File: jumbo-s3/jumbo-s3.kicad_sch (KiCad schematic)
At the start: 21 parts, among them U1 ESP32-S3, U2 APS12808L-3OBM-BA, U3 W25Q128JVS

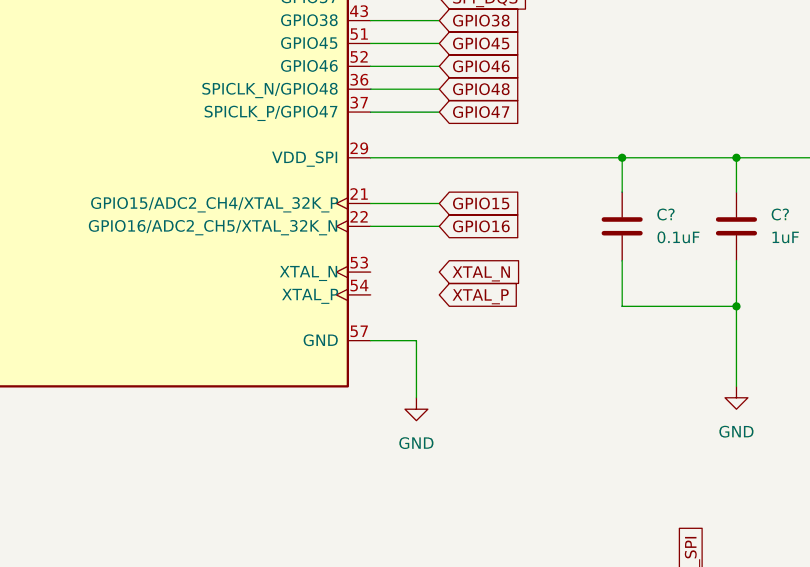
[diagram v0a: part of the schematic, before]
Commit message: schematic: add uC, flash and PSRAM
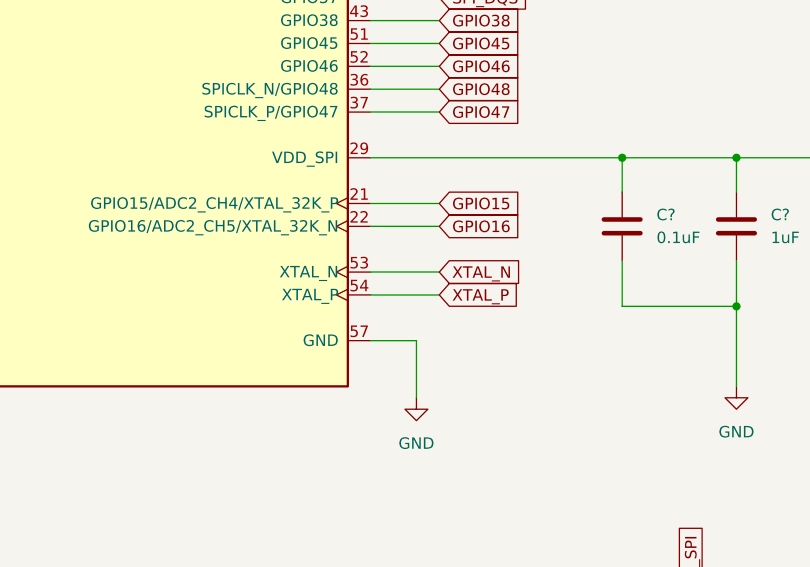
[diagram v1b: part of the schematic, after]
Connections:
- net XTAL_N: now also U1.53 (XTAL_N)
- net XTAL_P: now also U1.54 (XTAL_P)
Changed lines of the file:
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@@
+    (stroke (width 0) (type default) (color 0 0 0 0))
+  )
+  (wire (pts (xy 134.62 100.33) (xy 142.24 100.33))
     (stroke (width 0) (type default) (color 0 0 0 0))
   )
@@
     (stroke (width 0) (type default) (color 0 0 0 0))
   )
+  (wire (pts (xy 134.62 102.87) (xy 142.24 102.87))
+    (stroke (width 0) (type default) (color 0 0 0 0))
+  )

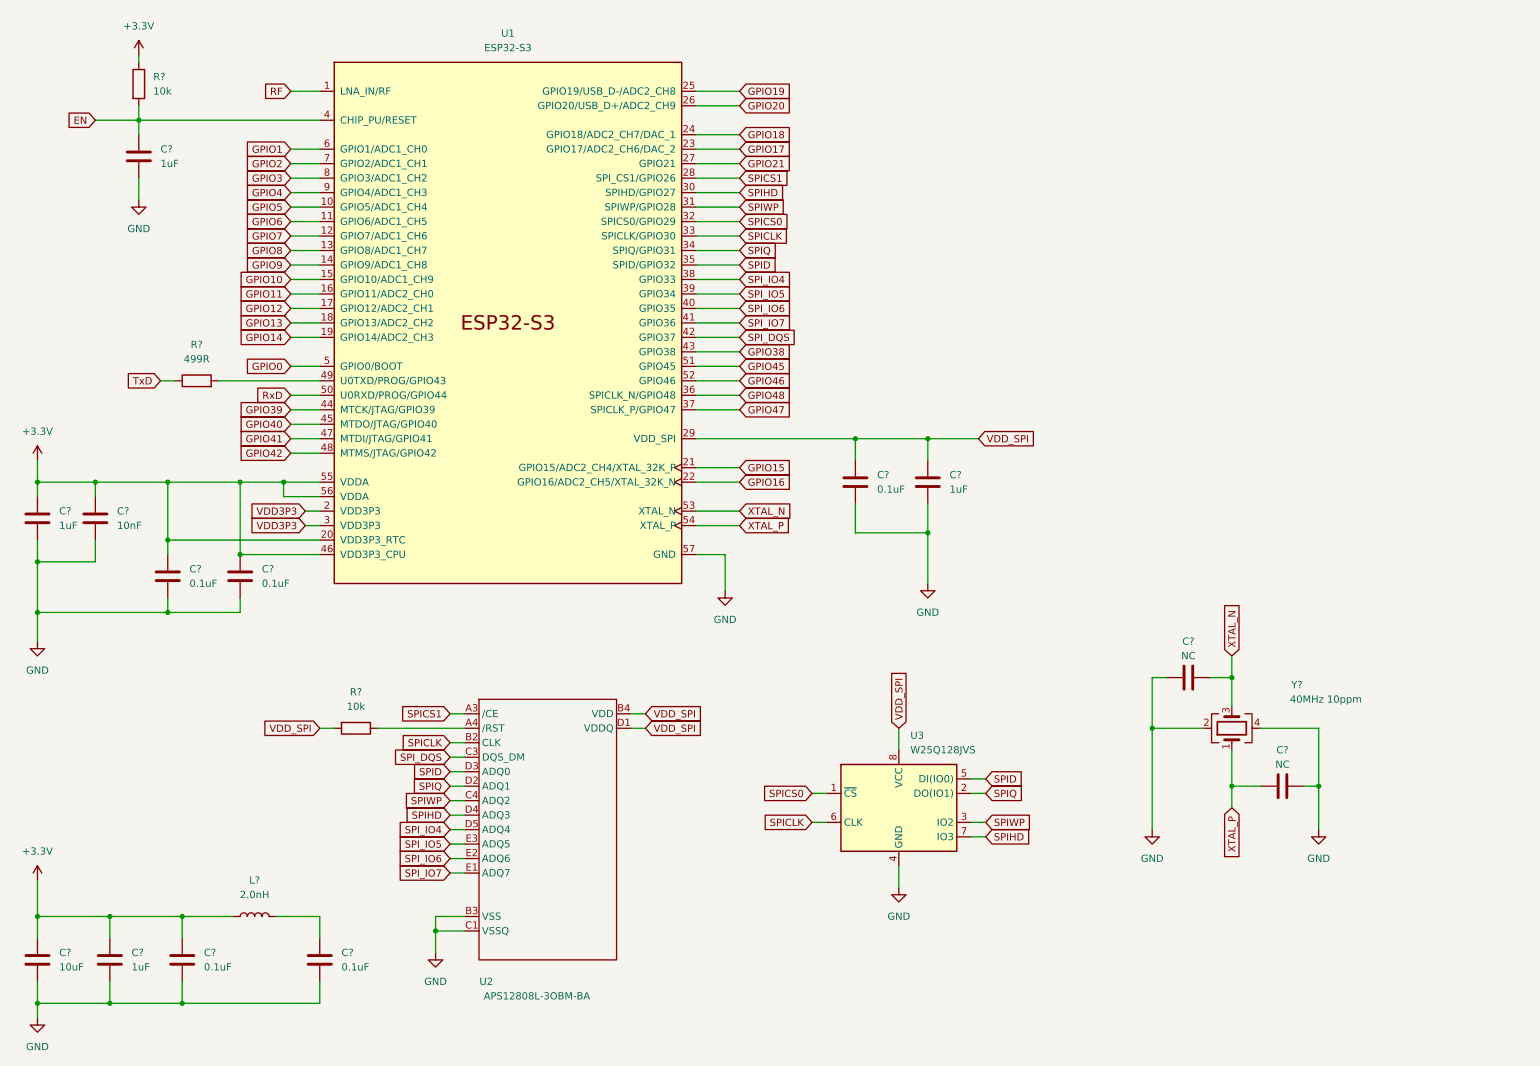
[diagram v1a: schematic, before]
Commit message: Finish schematic
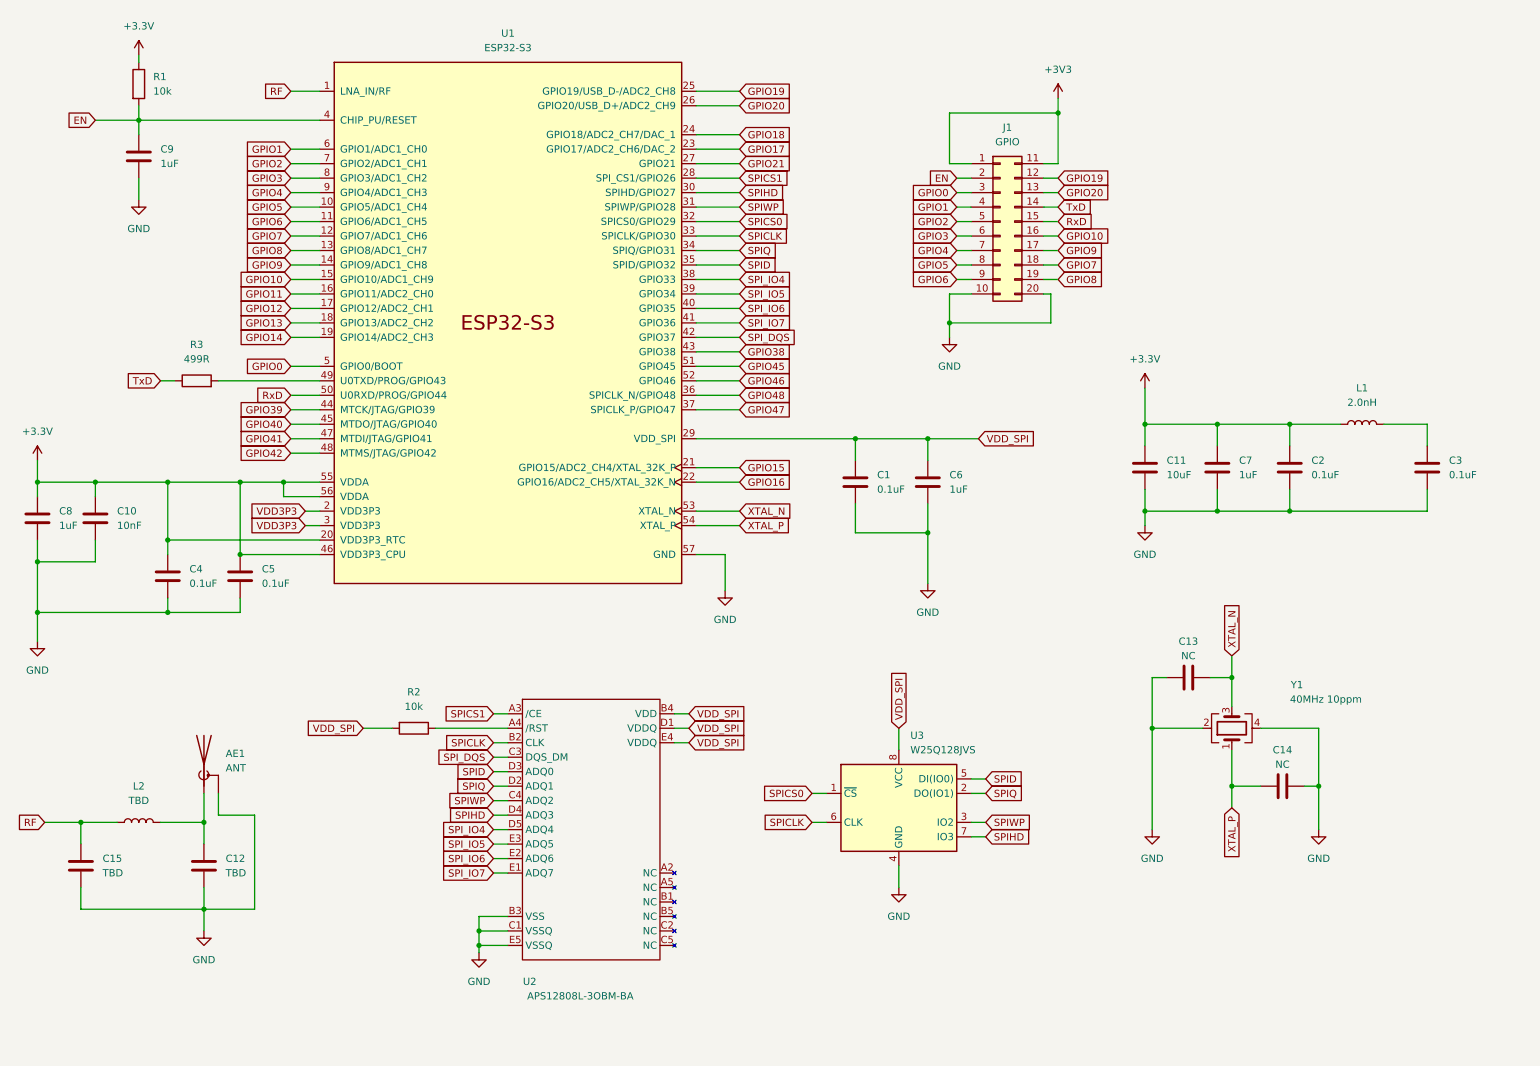
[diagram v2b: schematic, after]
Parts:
- added AE1: ANT, RF_Antenna:Texas_SWRA117D_2.4GHz_Left, symbol Device:Antenna_Shield
- added C12, C15: TBD, Capacitor_SMD:C_0603_1608Metric_Pad1.08x0.95mm_HandSolder, symbol Device:C
- added J1: GPIO, Connector_PinHeader_2.54mm:PinHeader_2x10_P2.54mm_Vertical_SMD, symbol Connector_Generic:Conn_02x10_Top_Bottom
- added L2: TBD, Inductor_SMD:L_0603_1608Metric_Pad1.05x0.95mm_HandSolder, symbol Device:L
- C1, C10, C11, C13, C14, C2, C3, C4, C5, C6, C7, C8, C9: renamed from C?; footprint (none) -> Capacitor_SMD:C_0603_1608Metric_Pad1.08x0.95mm_HandSolder
- L1: renamed from L?; footprint (none) -> Inductor_SMD:L_0603_1608Metric_Pad1.05x0.95mm_HandSolder
- R1, R2, R3: renamed from R?; footprint (none) -> Resistor_SMD:R_0603_1608Metric_Pad0.98x0.95mm_HandSolder
- Y1: renamed from Y?; footprint (none) -> Crystal:Crystal_SMD_3225-4Pin_3.2x2.5mm_HandSoldering
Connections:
- net EN: now also J1.2 (Pin_2)
- net GND: now also U2.E5 (VSSQ), AE1.2 (Shield), C12.2, C15.1, J1.10 (Pin_10), J1.20 (Pin_20)
- net GPIO0: now also J1.3 (Pin_3)
- net GPIO1: now also J1.4 (Pin_4)
- net GPIO10: now also J1.16 (Pin_16)
- net GPIO19: now also J1.12 (Pin_12)
- net GPIO2: now also J1.5 (Pin_5)
- net GPIO20: now also J1.13 (Pin_13)
- net GPIO3: now also J1.6 (Pin_6)
- net GPIO4: now also J1.7 (Pin_7)
- net GPIO5: now also J1.8 (Pin_8)
- net GPIO6: now also J1.9 (Pin_9)
- net GPIO7: now also J1.18 (Pin_18)
- net GPIO8: now also J1.19 (Pin_19)
- net GPIO9: now also J1.17 (Pin_17)
- net RF: now also C15.2, L2.1
- net RxD: now also J1.15 (Pin_15)
- net TxD: now also J1.14 (Pin_14)
- net VDD_SPI: now also U2.E4 (VDDQ)
- new net: AE1.1 (A), C12.1, L2.2
- new net +3V3: J1.1 (Pin_1), J1.11 (Pin_11)
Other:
- moved on the sheet: C11, C2, C3, C7, L1, R2

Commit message: pcb: rev. 1
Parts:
- removed J1: GPIO, Connector_PinHeader_2.54mm:PinHeader_2x10_P2.54mm_Vertical_SMD, symbol Connector_Generic:Conn_02x10_Top_Bottom
- removed U3: W25Q128JVS, Package_SO:SOIC-8_5.23x5.23mm_P1.27mm, symbol Memory_Flash:W25Q128JVS
- added J1: UART, Connector_PinHeader_2.54mm:PinHeader_1x04_P2.54mm_Vertical, symbol Connector:Conn_01x04_Male
- added J2: GPIO, Connector_PinSocket_2.54mm:PinSocket_1x12_P2.54mm_Vertical, symbol Connector:Conn_01x12_Male
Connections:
- net +3.3V: now also J1.1 (Pin_1), J2.6 (Pin_6)
- net EN: now also J2.12 (Pin_12)
- net GND: now also J1.4 (Pin_4), J2.5 (Pin_5)
- net GPIO0: now also J2.11 (Pin_11)
- net GPIO10: now also J2.10 (Pin_10)
- net GPIO11: now also J2.9 (Pin_9)
- net GPIO12: now also J2.8 (Pin_8)
- net GPIO13: now also J2.7 (Pin_7)
- net GPIO14: now also J2.4 (Pin_4)
- net GPIO15: now also J2.3 (Pin_3)
- net GPIO19: now also J2.2 (Pin_2)
- net GPIO20: now also J2.1 (Pin_1)
- net RxD: now also J1.3 (Pin_3)
- net TxD: now also J1.2 (Pin_2)
- net VDD3P3: now also C3.1, L1.2
- net GPIO1: no longer names the net of U1.6 (GPIO1/ADC1_CH0)
- net GPIO16: no longer names the net of U1.22 (GPIO16/ADC2_CH5/XTAL_32K_N)
- net GPIO17: no longer names the net of U1.23 (GPIO17/ADC2_CH6/DAC_2)
- net GPIO18: no longer names the net of U1.24 (GPIO18/ADC2_CH7/DAC_1)
- net GPIO2: no longer names the net of U1.7 (GPIO2/ADC1_CH1)
- net GPIO21: no longer names the net of U1.27 (GPIO21)
- net GPIO3: no longer names the net of U1.8 (GPIO3/ADC1_CH2)
- net GPIO38: no longer names the net of U1.43 (GPIO38)
- net GPIO39: no longer names the net of U1.44 (MTCK/JTAG/GPIO39)
- net GPIO4: no longer names the net of U1.9 (GPIO4/ADC1_CH3)
- net GPIO40: no longer names the net of U1.45 (MTDO/JTAG/GPIO40)
- net GPIO41: no longer names the net of U1.47 (MTDI/JTAG/GPIO41)
- net GPIO42: no longer names the net of U1.48 (MTMS/JTAG/GPIO42)
- net GPIO45: no longer names the net of U1.51 (GPIO45)
- net GPIO46: no longer names the net of U1.52 (GPIO46)
- net GPIO47: no longer names the net of U1.37 (SPICLK_P/GPIO47)
- net GPIO48: no longer names the net of U1.36 (SPICLK_N/GPIO48)
- net GPIO5: no longer names the net of U1.10 (GPIO5/ADC1_CH4)
- net GPIO6: no longer names the net of U1.11 (GPIO6/ADC1_CH5)
- net GPIO7: no longer names the net of U1.12 (GPIO7/ADC1_CH6)
- net GPIO8: no longer names the net of U1.13 (GPIO8/ADC1_CH7)
- net GPIO9: no longer names the net of U1.14 (GPIO9/ADC1_CH8)
- net SPICS0: no longer names the net of U1.32 (SPICS0/GPIO29)
- no-connect marks 0 -> 21

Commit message: Rev 2: init
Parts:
- removed J1: UART, Connector_PinHeader_2.54mm:PinHeader_1x04_P2.54mm_Vertical, symbol Connector:Conn_01x04_Male
- removed J2: GPIO, Connector_PinSocket_2.54mm:PinSocket_1x12_P2.54mm_Vertical, symbol Connector:Conn_01x12_Male
- added J1: GPIO, Connector_PinHeader_1.27mm:PinHeader_2x15_P1.27mm_Vertical_SMD, symbol Connector_Generic:Conn_02x15_Odd_Even
- added J2: DEBUG, symbol Connector_Generic:Conn_02x03_Odd_Even
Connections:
- net +3.3V: now also J1.1 (Pin_1), J1.11 (Pin_11), J1.13 (Pin_13), J1.2 (Pin_2), J2.1 (Pin_1)
- net EN: now also J2.3 (Pin_3)
- net GND: now also J1.14 (Pin_14), J1.15 (Pin_15), J1.29 (Pin_29), J1.30 (Pin_30), J2.6 (Pin_6)
- net GPIO0: now also J1.3 (Pin_3), J2.5 (Pin_5)
- net GPIO10: now also J1.4 (Pin_4)
- net GPIO11: now also J1.6 (Pin_6)
- net GPIO12: now also J1.8 (Pin_8)
- net GPIO13: now also J1.10 (Pin_10)
- net GPIO14: now also J1.12 (Pin_12)
- net GPIO15: now also J1.16 (Pin_16)
- net GPIO19: now also J1.24 (Pin_24)
- net GPIO20: now also J1.26 (Pin_26)
- net RxD: now also J2.4 (Pin_4)
- net TxD: now also J2.2 (Pin_2)
- net GPIO5: now reaches U1.10 (GPIO5/ADC1_CH4)
- net GPIO5: now also J1.25 (Pin_25)
- net GPIO6: now reaches U1.11 (GPIO6/ADC1_CH5)
- net GPIO6: now also J1.23 (Pin_23)
- net GPIO7: now reaches U1.12 (GPIO7/ADC1_CH6)
- net GPIO7: now also J1.21 (Pin_21)
- net GPIO8: now reaches U1.13 (GPIO8/ADC1_CH7)
- net GPIO8: now also J1.19 (Pin_19)
- net GPIO9: now reaches U1.14 (GPIO9/ADC1_CH8)
- net GPIO9: now also J1.17 (Pin_17)
- net GPIO16: now reaches U1.22 (GPIO16/ADC2_CH5/XTAL_32K_N)
- net GPIO16: now also J1.18 (Pin_18)
- net GPIO17: now reaches U1.23 (GPIO17/ADC2_CH6/DAC_2)
- net GPIO17: now also J1.20 (Pin_20)
- net GPIO18: now reaches U1.24 (GPIO18/ADC2_CH7/DAC_1)
- net GPIO18: now also J1.22 (Pin_22)
- net GPIO21: now reaches U1.27 (GPIO21)
- net GPIO21: now also J1.28 (Pin_28)
- net GPIO1: now reaches U1.6 (GPIO1/ADC1_CH0)
- net GPIO1: now also J1.5 (Pin_5)
- net GPIO2: now reaches U1.7 (GPIO2/ADC1_CH1)
- net GPIO2: now also J1.7 (Pin_7)
- net GPIO3: now reaches U1.8 (GPIO3/ADC1_CH2)
- net GPIO3: now also J1.9 (Pin_9)
- net GPIO4: now reaches U1.9 (GPIO4/ADC1_CH3)
- net GPIO4: now also J1.27 (Pin_27)
- no-connect marks 21 -> 4
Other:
- moved on the sheet: C11, C2, C3, C7, L1

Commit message: rev2: pcb: connect everything up
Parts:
- removed J2: DEBUG, symbol Connector_Generic:Conn_02x03_Odd_Even
- added J2: DEBUG, Connector_PinHeader_1.27mm:PinHeader_2x08_P1.27mm_Vertical_SMD, symbol Connector_Generic:Conn_02x08_Odd_Even
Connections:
- net +3.3V: now also J2.1 (Pin_1), J2.3 (Pin_3)
- net EN: now also J2.7 (Pin_7)
- net GND: now also J2.15 (Pin_15)
- net GPIO0: now also J2.9 (Pin_9)
- net RxD: now also J2.2 (Pin_2)
- net TxD: now also J2.5 (Pin_5)
- net GPIO48: now reaches U1.36 (SPICLK_N/GPIO48)
- net GPIO48: now also J2.13 (Pin_13)
- net GPIO47: now reaches U1.37 (SPICLK_P/GPIO47)
- net GPIO47: now also J2.11 (Pin_11)
- net GPIO38: now reaches U1.43 (GPIO38)
- net GPIO38: now also J2.16 (Pin_16)
- net GPIO39: now reaches U1.44 (MTCK/JTAG/GPIO39)
- net GPIO39: now also J2.14 (Pin_14)
- net GPIO40: now reaches U1.45 (MTDO/JTAG/GPIO40)
- net GPIO40: now also J2.12 (Pin_12)
- net GPIO41: now reaches U1.47 (MTDI/JTAG/GPIO41)
- net GPIO41: now also J2.10 (Pin_10)
- net GPIO42: now reaches U1.48 (MTMS/JTAG/GPIO42)
- net GPIO42: now also J2.8 (Pin_8)
- net GPIO45: now reaches U1.51 (GPIO45)
- net GPIO45: now also J2.6 (Pin_6)
- net GPIO46: now reaches U1.52 (GPIO46)
- net GPIO46: now also J2.4 (Pin_4)
- no-connect marks 4 -> 1

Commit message: Rev 2.1: unify headers
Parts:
- removed J1: GPIO, Connector_PinHeader_1.27mm:PinHeader_2x15_P1.27mm_Vertical_SMD, symbol Connector_Generic:Conn_02x15_Odd_Even
- removed J2: DEBUG, Connector_PinHeader_1.27mm:PinHeader_2x08_P1.27mm_Vertical_SMD, symbol Connector_Generic:Conn_02x08_Odd_Even
- added J1: GPIO, Connector_PinHeader_1.27mm:PinHeader_2x22_P1.27mm_Vertical_SMD, symbol Connector_Generic:Conn_02x22_Odd_Even
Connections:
- net +3.3V: now also J1.1 (Pin_1), J1.11 (Pin_11), J1.13 (Pin_13), J1.14 (Pin_14), J1.2 (Pin_2)
- net EN: now also J1.31 (Pin_31)
- net GND: now also J1.15 (Pin_15), J1.33 (Pin_33), J1.39 (Pin_39), J1.41 (Pin_41), J1.43 (Pin_43)
- net GPIO0: now also J1.3 (Pin_3)
- net GPIO1: now also J1.5 (Pin_5)
- net GPIO10: now also J1.4 (Pin_4)
- net GPIO11: now also J1.6 (Pin_6)
- net GPIO12: now also J1.8 (Pin_8)
- net GPIO13: now also J1.10 (Pin_10)
- net GPIO14: now also J1.12 (Pin_12)
- net GPIO15: now also J1.16 (Pin_16)
- net GPIO16: now also J1.18 (Pin_18)
- net GPIO17: now also J1.20 (Pin_20)
- net GPIO18: now also J1.22 (Pin_22)
- net GPIO19: now also J1.24 (Pin_24)
- net GPIO2: now also J1.7 (Pin_7)
- net GPIO20: now also J1.26 (Pin_26)
- net GPIO21: now also J1.28 (Pin_28)
- net GPIO3: now also J1.9 (Pin_9)
- net GPIO38: now also J1.44 (Pin_44)
- net GPIO39: now also J1.42 (Pin_42)
- net GPIO4: now also J1.27 (Pin_27)
- net GPIO40: now also J1.40 (Pin_40)
- net GPIO41: now also J1.38 (Pin_38)
- net GPIO42: now also J1.36 (Pin_36)
- net GPIO45: now also J1.34 (Pin_34)
- net GPIO46: now also J1.32 (Pin_32)
- net GPIO47: now also J1.37 (Pin_37)
- net GPIO48: now also J1.35 (Pin_35)
- net GPIO5: now also J1.25 (Pin_25)
- net GPIO6: now also J1.23 (Pin_23)
- net GPIO7: now also J1.21 (Pin_21)
- net GPIO8: now also J1.19 (Pin_19)
- net GPIO9: now also J1.17 (Pin_17)
- net RxD: now also J1.30 (Pin_30)
- net TxD: now also J1.29 (Pin_29)
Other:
- moved on the sheet: C11, C13, C14, C2, C3, C7, L1, Y1
